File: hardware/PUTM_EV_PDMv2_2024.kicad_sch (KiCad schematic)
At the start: 13 parts, among them J6 FTSH-107-01-L-DV-K-A, J7 USB_C_Receptacle_USB2.0_14P, U1 STM32G0C1KCTxN

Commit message: NEW SCHEMATIC
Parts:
- removed C1, C3: 100n, Capacitor_SMD:C_0603_1608Metric, symbol Device:C_Small
- removed C2, C4: 4.7u, Capacitor_SMD:C_0603_1608Metric, symbol Device:C_Small
- removed C53: 10n, Capacitor_SMD:C_0603_1608Metric_Pad1.08x0.95mm_HandSolder, symbol Device:C_Small
- removed D12: TPD2E2U06QDCKRQ1, Package_TO_SOT_SMD:SOT-323_SC-70_Handsoldering, symbol Device:D_TVS_Dual_AAC
- removed J6: FTSH-107-01-L-DV-K-A, FTSH-107-XX-YYY-DV-K-A, symbol FTSH-107-01-L-DV-K-A:FTSH-107-01-L-DV-K-A
- removed J7: USB_C_Receptacle_USB2.0_14P, Connector_USB:USB_C_Receptacle_JAE_DX07S024WJ3R400, symbol usb_c_receptacle_usb2.0_14p:USB_C_Receptacle_USB2.0_14P
- removed R19: 100k, Resistor_SMD:R_0603_1608Metric, symbol Device:R_Small
- removed R20: 0, Resistor_SMD:R_0603_1608Metric_Pad0.98x0.95mm_HandSolder, symbol Device:R_Small
- removed R22, R23: 5.1k, Resistor_SMD:R_0603_1608Metric_Pad0.98x0.95mm_HandSolder, symbol Device:R_Small
- removed U1: STM32G0C1KCTxN, Package_QFP:LQFP-32_7x7mm_P0.8mm, symbol MCU_ST_STM32G0:STM32G0C1KCTxN
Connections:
- no-connect marks 9 -> 0
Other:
- sheet Controllers renamed Power controllers
- removed sheet LEDs
- added sheet MCU (mcu.kicad_sch)
- sheet CAN ports: added CAN_GND_ISO, CAN{N P}, CAN{RX TX}, STBY_CAN; removed CAN_H, CAN_L, CAN_RX, CAN_TX
- sheet Connectors ports: added CAN_GND_ISO, CAN{N P}, RST, SW{CLK DIO}, USART{TX RX}, USB{- +}; removed none
- sheet Power controllers ports: added FUSE_IS[0..3], LHI[0..3], SPI{NSS SCK MISO MOSI}; removed CSN, IS_1, IS_2, IS_3, IS_4, LHI_1, LHI_2, LHI_3, LHI_4, MISO, MOSI, SCLK
- note added: "Isolated"
- note added: "PDMv3"
- note removed: "CAN"
- note removed: "Connectors"
- note removed: "LEDs"
- note removed: "Power"
- note removed: "Power ICs"
- note removed: "Programmer"
- note removed: "STM32"
- note removed: "USB C connector"
- company: Author: -> Authors: Grzegorz Potocki Jędrzej Kasprzyk
- title: (none) -> PDUv3

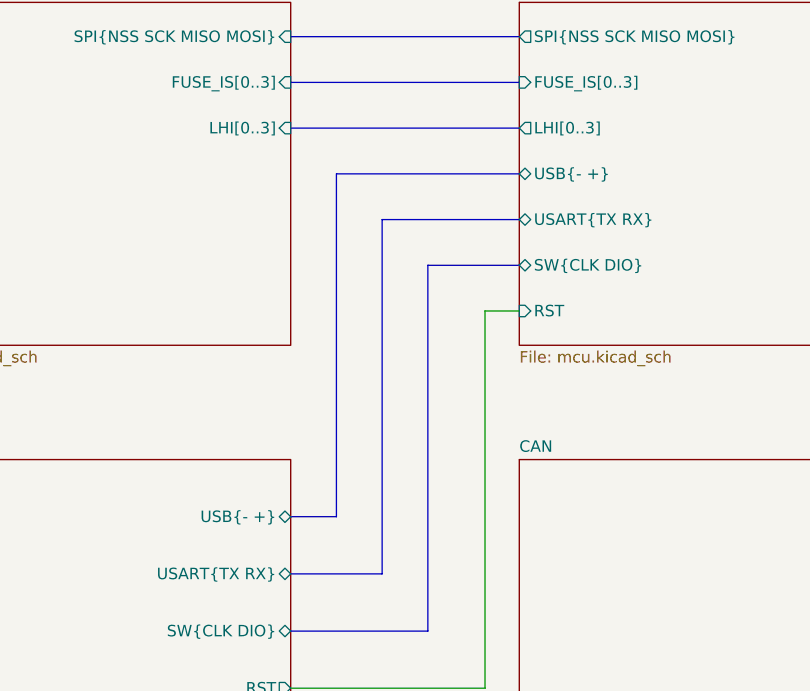
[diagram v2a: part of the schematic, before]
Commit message: pcb layout-power section 5V update
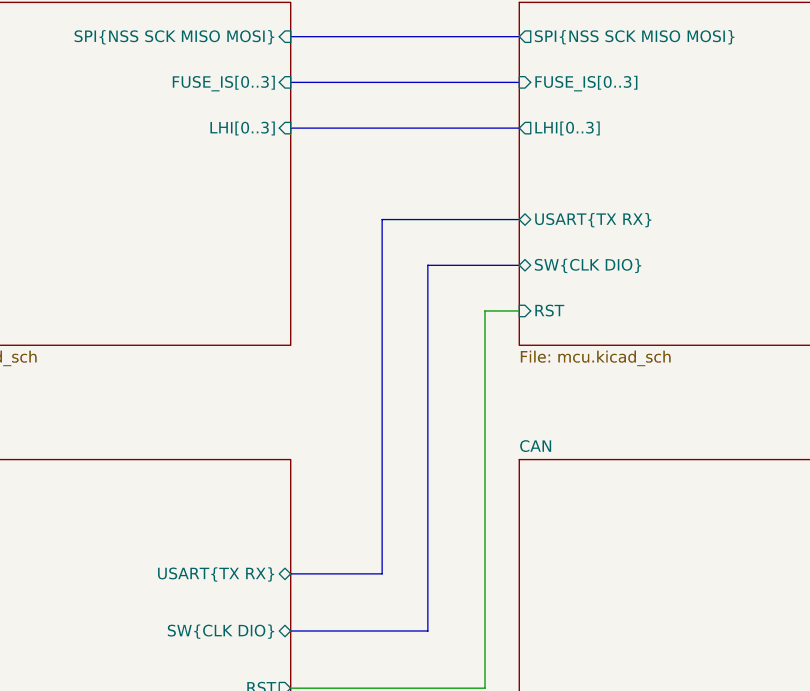
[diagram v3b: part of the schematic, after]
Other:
- sheet Connectors ports: added none; removed USB{- +}
- sheet MCU ports: added none; removed USB{- +}
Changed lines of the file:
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@@
-	(bus
-		(pts
-			(xy 106.68 120.65) (xy 106.68 82.55)
-		)
-		(stroke
-			(width 0)
-			(type default)
-		)
-	)
 	(bus
 		(pts
@@
 	(bus
 		(pts
-			(xy 101.6 120.65) (xy 106.68 120.65)
-		)
-		(stroke
-			(width 0)
-			(type default)
-		)
-	)
-	(bus
-		(pts
 			(xy 101.6 77.47) (xy 127 77.47)
 		)
@@
 		(pts
 			(xy 116.84 92.71) (xy 127 92.71)
-		)
-		(stroke
-			(width 0)
-			(type default)
-		)
-	)
-	(bus
-		(pts
-			(xy 106.68 82.55) (xy 127 82.55)
 		)
 		(stroke
@@
 			)
 		)
-		(pin "USB{- +}" bidirectional
-			(at 127 82.55 180)
-			(effects
-				(font
-					(size 1.27 1.27)
-				)
-				(justify left)
-			)
-		)
 		(pin "FUSE_IS[0..3]" input
 			(at 127 72.39 180)
@@
 			(effects
 				(font
-					(size 1.27 1.27)
-				)
-				(justify right)
-			)
-		)
-		(pin "USB{- +}" bidirectional
-			(at 101.6 120.65 0)
-			(effects
-				(font
